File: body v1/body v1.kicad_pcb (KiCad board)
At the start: 2 copper layers, 98 x 69 mm, 85 parts, among them IC1 Con_I2C, IC2 Con_I2C, IC3 Con_I2C, IC4 Con_I2C, J2 BAU, K1 G2RL-1-E, P1 Conn_01x02, P2 Conn_01x02, P3 Conn_01x02, P4 Conn_01x02, P5 XT30, P6 XT30, U1 TSR1-2433E, U2 TSR1-2450E, X1 ESP32

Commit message: debut dessin
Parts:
- added G***: LOGO, LOGO, F.Cu at (128.8, 100.0)
- added G***: LOGO, LOGO, F.Cu at (189.1, 83.1)
- added G***: LOGO, LOGO, F.Cu at (197.0, 91.1)
- added G***: LOGO, LOGO, F.Cu at (181.1, 91.1)
- added G***: LOGO, LOGO, B.Cu at (205.0, 91.1)
- added G***: LOGO, LOGO, B.Cu at (205.0, 83.1)
- added G***: LOGO, LOGO, B.Cu at (197.0, 91.1)
- added G***: LOGO, LOGO, B.Cu at (189.1, 91.1)
- added G***: LOGO, LOGO, B.Cu at (197.0, 83.1)
- added G***: LOGO, LOGO, B.Cu at (189.1, 83.1)
- added G***: LOGO, LOGO, B.Cu at (181.1, 91.1)
- added G***: LOGO, LOGO, F.Cu at (116.8, 57.1)
- added G***: LOGO, LOGO, B.Cu at (129.5, 105.4)
- added G***: LOGO, LOGO, B.Cu at (187.5, 71.2)
- added G***: LOGO, LOGO, B.Cu at (202.5, 71.2)
- added G***: LOGO, LOGO, B.Cu at (207.2, 100.5)
- added G***: LOGO, LOGO, B.Cu at (151.2, 48.9)
- added G***: LOGO, LOGO, B.Cu at (181.1, 83.1)
- added G***: LOGO, LOGO, B.Cu at (172.5, 71.2)
- added G***: LOGO, LOGO, F.Cu at (181.1, 83.1)
- added G***: LOGO, LOGO, F.Cu at (205.0, 91.1)
- added G***: LOGO, LOGO, F.Cu at (134.6, 100.9)
- added G***: LOGO, LOGO, F.Cu at (207.2, 98.4)
- added G***: LOGO, LOGO, F.Cu at (205.0, 83.1)
- added G***: LOGO, LOGO, F.Cu at (197.0, 83.1)
- added G***: LOGO, LOGO, F.Cu at (189.1, 91.1)
- added kibuzzard-690E9406: G***, kibuzzard-690E9406, F.Cu at (122.0, 49.8)
- added kibuzzard-690E9406: G***, kibuzzard-690E9406, F.Cu at (127.5, 49.8)
- added kibuzzard-690E9406: G***, kibuzzard-690E9406, F.Cu at (124.7, 49.8)
- added kibuzzard-690E9406: G***, kibuzzard-690E9406, F.Cu at (133.2, 49.8)
- added kibuzzard-690E9406: G***, kibuzzard-690E9406, F.Cu at (130.2, 49.8)
- added kibuzzard-690E943A: G***, kibuzzard-690E943A, F.Cu at (131.3, 49.8)
- added kibuzzard-690E943A: G***, kibuzzard-690E943A, F.Cu at (123.0, 49.8)
- added kibuzzard-690E943A: G***, kibuzzard-690E943A, F.Cu at (128.5, 49.8)
- added kibuzzard-690E943A: G***, kibuzzard-690E943A, F.Cu at (125.8, 49.8)
- added kibuzzard-690E943A: G***, kibuzzard-690E943A, F.Cu at (134.2, 49.8)
- added kibuzzard-69B800EA: G***, kibuzzard-69B800EA, F.Cu at (198.4, 70.0)
- added kibuzzard-69B80110: G***, kibuzzard-69B80110, F.Cu at (168.9, 70.0)
- added kibuzzard-69B80117: G***, kibuzzard-69B80117, F.Cu at (183.4, 70.0)
- added kibuzzard-69BAE0CF: G***, kibuzzard-69BAE0CF, F.Cu at (163.7, 46.4)
- added kibuzzard-69BAE350: G***, kibuzzard-69BAE350, F.Cu at (163.7, 47.6)
- added kibuzzard-69BAE35E: G***, kibuzzard-69BAE35E, F.Cu at (163.7, 48.9)
- added kibuzzard-69BAE367: G***, kibuzzard-69BAE367, F.Cu at (163.7, 50.2)
- added kibuzzard-69BAE380: G***, kibuzzard-69BAE380, F.Cu at (163.7, 51.4)
- added kibuzzard-69BAE387: G***, kibuzzard-69BAE387, F.Cu at (163.7, 52.7)
- added kibuzzard-69BAE38F: G***, kibuzzard-69BAE38F, F.Cu at (163.7, 54.0)
- added kibuzzard-69BAE395: G***, kibuzzard-69BAE395, F.Cu at (163.7, 60.3)
- added kibuzzard-69BAE431: G***, kibuzzard-69BAE431, F.Cu at (163.7, 59.1)
- added kibuzzard-69BAE443: G***, kibuzzard-69BAE443, F.Cu at (163.7, 56.5)
- added kibuzzard-69BAE476: G***, kibuzzard-69BAE476, F.Cu at (163.7, 61.6)
- added kibuzzard-69BAE48B: G***, kibuzzard-69BAE48B, F.Cu at (151.0, 61.6)
- added kibuzzard-69BAE4CB: G***, kibuzzard-69BAE4CB, F.Cu at (151.0, 60.3)
- added kibuzzard-69BAE4D9: G***, kibuzzard-69BAE4D9, F.Cu at (151.0, 59.1)
- added kibuzzard-69BAE4E7: G***, kibuzzard-69BAE4E7, F.Cu at (151.0, 57.8)
- added kibuzzard-69BAE4F1: G***, kibuzzard-69BAE4F1, F.Cu at (151.0, 56.5)
- added kibuzzard-69BAE75D: G***, kibuzzard-69BAE75D, F.Cu at (116.1, 62.4)
- added kibuzzard-69BAE75D: G***, kibuzzard-69BAE75D, F.Cu at (161.2, 59.1)
- added kibuzzard-69BAE75D: G***, kibuzzard-69BAE75D, B.Cu at (195.6, 49.5)
- added kibuzzard-69BAE766: G***, kibuzzard-69BAE766, F.Cu at (161.2, 56.5)
- added kibuzzard-69BAE766: G***, kibuzzard-69BAE766, F.Cu at (116.1, 59.8)
- added kibuzzard-69BAE766: G***, kibuzzard-69BAE766, B.Cu at (195.6, 50.8)
- added kibuzzard-69BAE772: G***, kibuzzard-69BAE772, F.Cu at (161.2, 61.6)
- added kibuzzard-69BAE77A: G***, kibuzzard-69BAE77A, F.Cu at (153.6, 61.6)
- added kibuzzard-69BAE799: G***, kibuzzard-69BAE799, F.Cu at (161.2, 55.2)
- added kibuzzard-69BAE7DC: G***, kibuzzard-69BAE7DC, F.Cu at (161.2, 57.8)
- added kibuzzard-69BAE836: G***, kibuzzard-69BAE836, F.Cu at (152.3, 55.2)
- added kibuzzard-69BAE8DD: G***, kibuzzard-69BAE8DD, F.Cu at (183.4, 66.9)
- added kibuzzard-69BAE8DD: G***, kibuzzard-69BAE8DD, F.Cu at (168.9, 66.9)
- added kibuzzard-69BAE8DD: G***, kibuzzard-69BAE8DD, F.Cu at (198.4, 66.9)
- added kibuzzard-69BAED5C: G***, kibuzzard-69BAED5C, B.Cu at (195.6, 43.2)
- added kibuzzard-69BAED6C: G***, kibuzzard-69BAED6C, B.Cu at (195.6, 44.5)
- added kibuzzard-69BAED73: G***, kibuzzard-69BAED73, B.Cu at (195.6, 45.7)
- added kibuzzard-69BAED80: G***, kibuzzard-69BAED80, B.Cu at (195.6, 47.0)
- added kibuzzard-69BAEDC3: G***, kibuzzard-69BAEDC3, B.Cu at (181.0, 44.5)
- added kibuzzard-69BAEDD0: G***, kibuzzard-69BAEDD0, B.Cu at (181.0, 45.7)
- added kibuzzard-69BAEDD6: G***, kibuzzard-69BAEDD6, B.Cu at (181.0, 47.0)
- added kibuzzard-69BAEDDC: G***, kibuzzard-69BAEDDC, B.Cu at (181.0, 48.3)
- added kibuzzard-69BAEEA0: G***, kibuzzard-69BAEEA0, B.Cu at (181.0, 49.5)
- added kibuzzard-69BAEEAC: G***, kibuzzard-69BAEEAC, B.Cu at (181.0, 50.8)
- added kibuzzard-69BAEEB4: G***, kibuzzard-69BAEEB4, B.Cu at (181.0, 52.1)
- added kibuzzard-69BAFB08: G***, kibuzzard-69BAFB08, F.Cu at (116.2, 54.7)
- added kibuzzard-69BAFC53: G***, kibuzzard-69BAFC53, F.Cu at (128.0, 47.0)
- added kibuzzard-69BAFC58: G***, kibuzzard-69BAFC58, F.Cu at (125.2, 47.0)
- added kibuzzard-69BAFC5E: G***, kibuzzard-69BAFC5E, F.Cu at (122.2, 47.0)
- added kibuzzard-69BAFC82: G***, kibuzzard-69BAFC82, F.Cu at (130.7, 47.0)
- added kibuzzard-69BAFCAD: G***, kibuzzard-69BAFCAD, F.Cu at (133.5, 47.0)
- added kibuzzard-69BAFD5E: G***, kibuzzard-69BAFD5E, F.Cu at (178.8, 86.7)
- added kibuzzard-69BAFD5E: G***, kibuzzard-69BAFD5E, F.Cu at (178.9, 78.7)
- added kibuzzard-69BAFE68: G***, kibuzzard-69BAFE68, F.Cu at (202.5, 78.7)
- added kibuzzard-69BAFE76: G***, kibuzzard-69BAFE76, F.Cu at (202.5, 86.7)
- added kibuzzard-69BAFF00: G***, kibuzzard-69BAFF00, F.Cu at (194.5, 78.7)
- added kibuzzard-69BAFF06: G***, kibuzzard-69BAFF06, F.Cu at (194.4, 86.7)
- moved L1 47.6 mm to (139.0, 42.9), turned to -90 degrees
- moved Bat1 46.9 mm to (125.6, 96.7)
- moved C1 46.9 mm to (201.0, 44.3)
- moved C6 46.9 mm to (172.0, 81.5)
- moved D4 46.9 mm to (143.0, 94.0)
- moved DRV1 46.9 mm to (198.0, 104.5)
- moved DRV2 46.9 mm to (198.0, 97.0)
- moved DT3 46.9 mm to (130.7, 44.0)
- moved DT5 46.9 mm to (133.7, 44.0)
- moved F1 46.9 mm to (124.5, 107.2)
- moved H3 46.9 mm to (206.5, 44.7)
- moved H4 46.9 mm to (206.5, 105.7)
- moved IC3 46.9 mm to (134.7, 54.7)
- moved IC4 46.9 mm to (142.7, 54.7)
- moved J2 46.9 mm to (134.6, 94.3)
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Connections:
- L1 pad 1: DIN-xbee -> DOUT-xbee
- L1 pad 2: DOUT-xbee -> DIN-xbee
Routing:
- net +24V: track 121.0 -> 141.5 mm
- net +3V3: track 273.9 -> 269.7 mm
- net DIN-xbee: track 39.9 -> 37.3 mm
- net DOUT-xbee: track 38.0 -> 36.0 mm
- net GND: vias 138 -> 137
- added copper zone on B.Cu, net +24V
- removed copper zone on F.Cu, net +24V

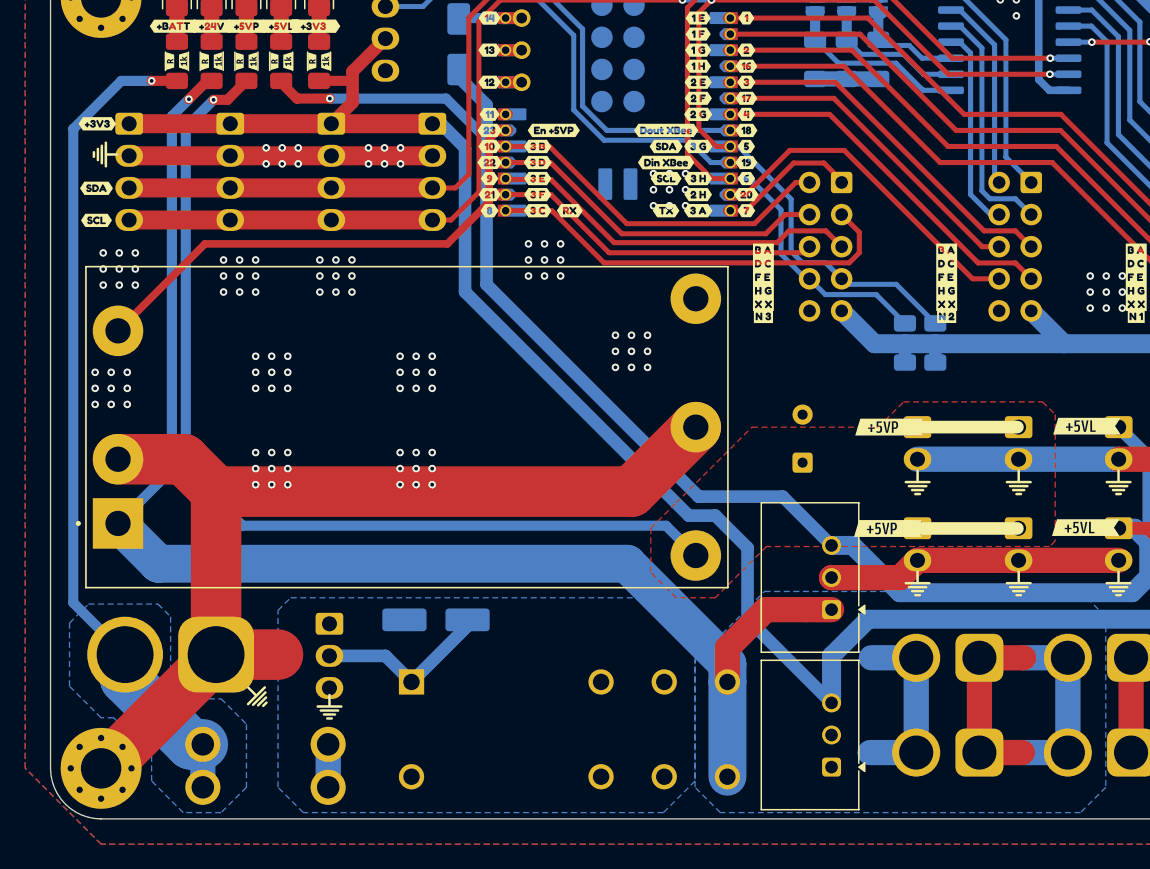
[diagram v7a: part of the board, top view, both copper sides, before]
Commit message: end of body +start of head
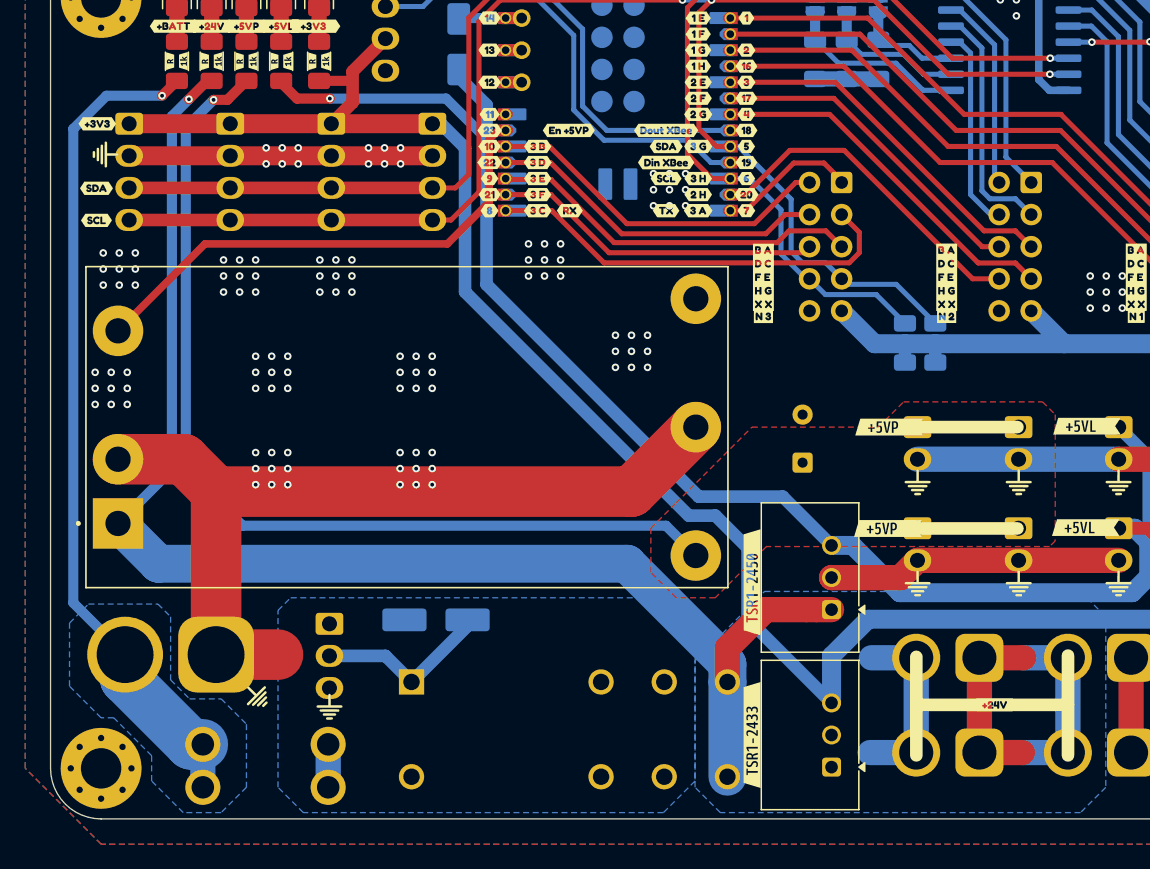
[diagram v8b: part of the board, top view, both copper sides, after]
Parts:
- added G***: LOGO, LOGO, B.Cu at (132.6, 36.0)
- added G***: LOGO, LOGO, B.Cu at (141.9, 65.9)
- added G***: LOGO, LOGO, B.Cu at (134.2, 89.3)
- added G***: LOGO, LOGO, B.Cu at (201.3, 99.6)
- added kibuzzard-69BBC5C3: G***, kibuzzard-69BBC5C3, F.Cu at (168.0, 103.1)
- added kibuzzard-69BBC5E5: G***, kibuzzard-69BBC5E5, F.Cu at (168.0, 91.0)
- added kibuzzard-69BCFD1C: G***, kibuzzard-69BCFD1C, F.Cu at (187.2, 100.7)
- moved kibuzzard-69BAE836 1.19 mm to (153.5, 55.2)
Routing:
- net GND: track 213.9 -> 201.4 mm
